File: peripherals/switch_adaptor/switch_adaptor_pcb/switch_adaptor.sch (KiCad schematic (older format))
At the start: 3 parts, among them J1 PJ320A, J2 PJ320A, J3 PJ320A

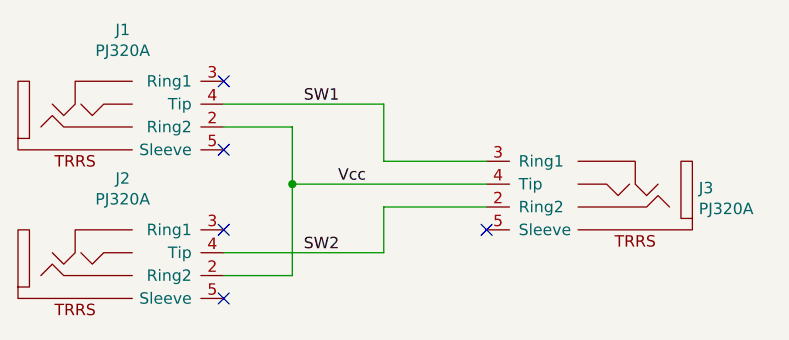
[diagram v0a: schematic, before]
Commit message: Updated switch adaptor design
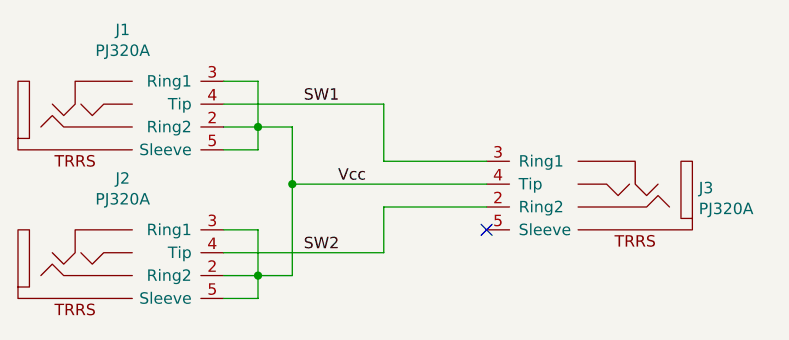
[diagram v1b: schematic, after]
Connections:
- net Vcc: now also J1.3 (Ring1), J1.5 (Sleeve), J2.3 (Ring1), J2.5 (Sleeve)
- no-connect marks 5 -> 1
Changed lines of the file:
@@
 Wire Wire Line
 	5075 3525 5525 3525
-NoConn ~ 4375 2975
-NoConn ~ 4375 3625
-NoConn ~ 4375 3925
-NoConn ~ 4375 3275
 NoConn ~ 5525 3625
 Wire Wire Line
-	4375 3175 4675 3175
-Wire Wire Line
-	4675 3175 4675 3425
+	4375 3175 4525 3175
 Wire Wire Line
 	4675 3425 5525 3425
 Wire Wire Line
-	4675 3425 4675 3825
-Wire Wire Line
-	4675 3825 4375 3825
+	4675 3825 4525 3825
 Connection ~ 4675 3425
 $Comp
@@
 Text Label 4725 3725 0    50   ~ 0
 SW2
+Wire Wire Line
+	4375 3275 4525 3275
+Wire Wire Line
+	4375 2975 4525 2975
+Wire Wire Line
+	4375 3625 4525 3625
+Wire Wire Line
+	4375 3925 4525 3925
+Wire Wire Line
+	4525 2975 4525 3175
+Connection ~ 4525 3175
+Wire Wire Line
+	4525 3175 4675 3175
+Wire Wire Line
+	4525 3175 4525 3275
+Wire Wire Line
+	4675 3175 4675 3425
+Wire Wire Line
+	4525 3625 4525 3825
+Connection ~ 4525 3825
+Wire Wire Line
+	4525 3825 4375 3825
+Wire Wire Line
+	4525 3825 4525 3925
+Wire Wire Line
+	4675 3425 4675 3825
 $EndSCHEMATC
